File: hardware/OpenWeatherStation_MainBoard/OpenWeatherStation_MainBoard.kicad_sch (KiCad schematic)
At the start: 0 parts

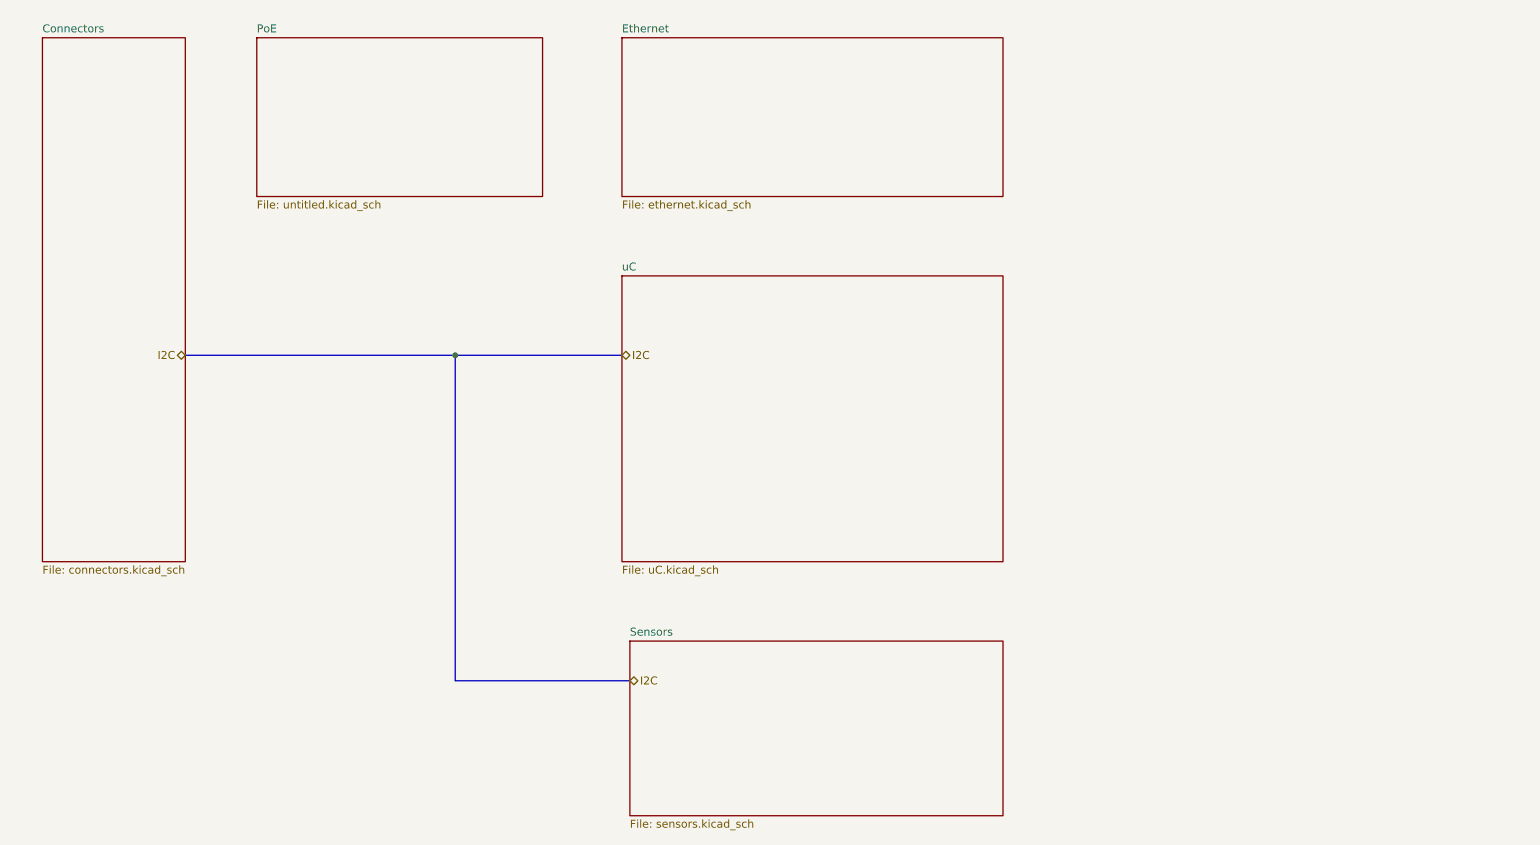
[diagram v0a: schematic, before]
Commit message: fix hierarchical bus
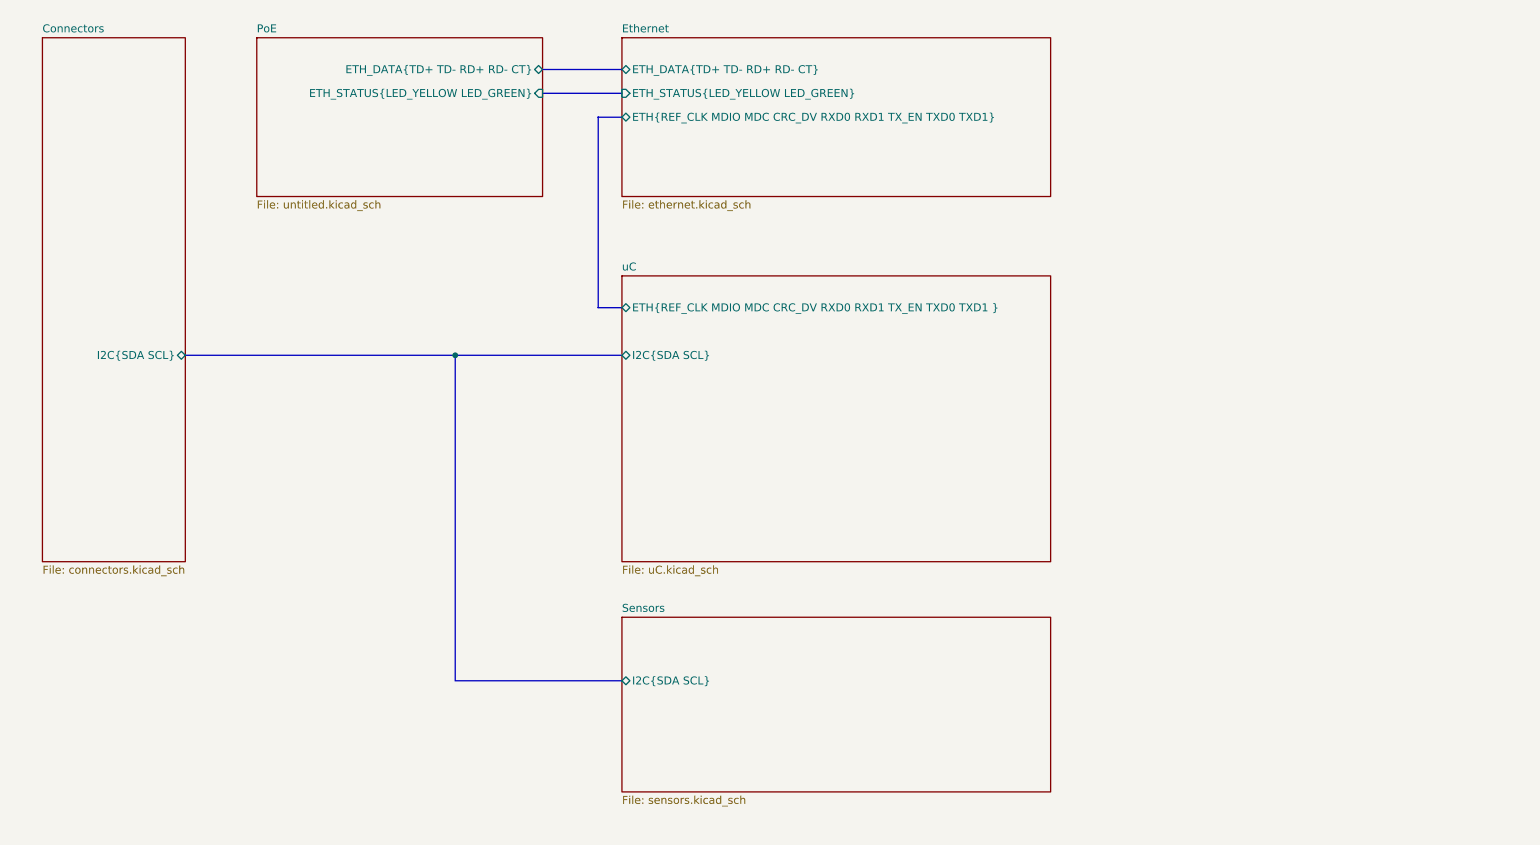
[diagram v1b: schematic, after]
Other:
- sheet Connectors ports: added I2C{SDA SCL}; removed none
- sheet Ethernet ports: added ETH_DATA{TD+ TD- RD+ RD- CT}, ETH_STATUS{LED_YELLOW LED_GREEN}, ETH{REF_CLK MDIO MDC CRC_DV RXD0 RXD1 TX_EN TXD0 TXD1}; removed none
- sheet PoE ports: added ETH_DATA{TD+ TD- RD+ RD- CT}, ETH_STATUS{LED_YELLOW LED_GREEN}; removed none
- sheet Sensors ports: added I2C{SDA SCL}; removed none
- sheet uC ports: added ETH{REF_CLK MDIO MDC CRC_DV RXD0 RXD1 TX_EN TXD0 TXD1 }, I2C{SDA SCL}; removed none
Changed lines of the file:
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@@
     (stroke (width 0) (type default))
   )
-  (bus (pts (xy 82.55 134.62) (xy 110.49 134.62))
+  (bus (pts (xy 105.41 44.45) (xy 105.41 74.93))
+    (stroke (width 0) (type default))
+  )
+  (bus (pts (xy 96.52 36.83) (xy 109.22 36.83))
+    (stroke (width 0) (type default))
+  )
+  (bus (pts (xy 109.22 44.45) (xy 105.41 44.45))
+    (stroke (width 0) (type default))
+  )
+  (bus (pts (xy 105.41 74.93) (xy 109.22 74.93))
+    (stroke (width 0) (type default))
+  )
+  (bus (pts (xy 82.55 134.62) (xy 109.22 134.62))
+    (stroke (width 0) (type default))
+  )
+  (bus (pts (xy 96.52 40.64) (xy 109.22 40.64))
     (stroke (width 0) (type default))
   )
@@
     (stroke (width 0) (type default))
   )
-  (hierarchical_label "I2C" (shape bidirectional) (at 109.22 82.55 0) (fields_autoplaced)
-    (effects (font (size 1.27 1.27)) (justify left))
-  )
-  (hierarchical_label "I2C" (shape bidirectional) (at 110.49 134.62 0) (fields_autoplaced)
-    (effects (font (size 1.27 1.27)) (justify left))
-  )
-  (hierarchical_label "I2C" (shape bidirectional) (at 39.37 82.55 180) (fields_autoplaced)
-    (effects (font (size 1.27 1.27)) (justify right))
-  )
-  (sheet (at 109.22 31.75) (size 60.96 25.4) (fields_autoplaced)
+  (sheet (at 109.22 31.75) (size 68.58 25.4) (fields_autoplaced)
     (stroke (width 0.1524) (type solid))
     (fill (color 0 0 0 0.0000))
@@
     (property "Sheetfile" "ethernet.kicad_sch" (at 109.22 57.7346 0)
       (effects (font (size 1.27 1.27)) (justify left top))
+    )
+    (pin "ETH_STATUS{LED_YELLOW LED_GREEN}" input (at 109.22 40.64 180)
+      (effects (font (size 1.27 1.27)) (justify left))
+    )
+    (pin "ETH_DATA{TD+ TD- RD+ RD- CT}" bidirectional (at 109.22 36.83 180)
+      (effects (font (size 1.27 1.27)) (justify left))
+    )
+    (pin "ETH{REF_CLK MDIO MDC CRC_DV RXD0 RXD1 TX_EN TXD0 TXD1}" bidirectional (at 109.22 44.45 180)
+      (effects (font (size 1.27 1.27)) (justify left))
     )
     (instances
@@
       (effects (font (size 1.27 1.27)) (justify left top))
     )
+    (pin "I2C{SDA SCL}" bidirectional (at 39.37 82.55 0)
+      (effects (font (size 1.27 1.27)) (justify right))
+    )
     (instances
       (project "OpenWeatherStation_MainBoard"
@@
       (effects (font (size 1.27 1.27)) (justify left top))
     )
+    (pin "ETH_STATUS{LED_YELLOW LED_GREEN}" input (at 96.52 40.64 0)
+      (effects (font (size 1.27 1.27)) (justify right))
+    )
+    (pin "ETH_DATA{TD+ TD- RD+ RD- CT}" bidirectional (at 96.52 36.83 0)
+      (effects (font (size 1.27 1.27)) (justify right))
+    )
     (instances
       (project "OpenWeatherStation_MainBoard"
@@
     )
   )
-  (sheet (at 110.49 128.27) (size 59.69 27.94) (fields_autoplaced)
+  (sheet (at 109.22 124.46) (size 68.58 27.94) (fields_autoplaced)
     (stroke (width 0.1524) (type solid))
     (fill (color 0 0 0 0.0000))
-    (property "Sheetname" "Sensors" (at 110.49 127.5584 0)
+    (property "Sheetname" "Sensors" (at 109.22 123.7484 0)
       (effects (font (size 1.27 1.27)) (justify left bottom))
     )
-    (property "Sheetfile" "sensors.kicad_sch" (at 110.49 156.7946 0)
+    (property "Sheetfile" "sensors.kicad_sch" (at 109.22 152.9846 0)
       (effects (font (size 1.27 1.27)) (justify left top))
+    )
+    (pin "I2C{SDA SCL}" bidirectional (at 109.22 134.62 180)
+      (effects (font (size 1.27 1.27)) (justify left))
     )
     (instances
@@
     )
   )
-  (sheet (at 109.22 69.85) (size 60.96 45.72) (fields_autoplaced)
+  (sheet (at 109.22 69.85) (size 68.58 45.72) (fields_autoplaced)
     (stroke (width 0.1524) (type solid))
     (fill (color 0 0 0 0.0000))
@@
       (effects (font (size 1.27 1.27)) (justify left top))
     )
+    (pin "I2C{SDA SCL}" bidirectional (at 109.22 82.55 180)
+      (effects (font (size 1.27 1.27)) (justify left))
+    )
+    (pin "ETH{REF_CLK MDIO MDC CRC_DV RXD0 RXD1 TX_EN TXD0 TXD1 }" bidirectional (at 109.22 74.93 180)
+      (effects (font (size 1.27 1.27)) (justify left))
+    )
     (instances

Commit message: move eth connector to dedicated sheet
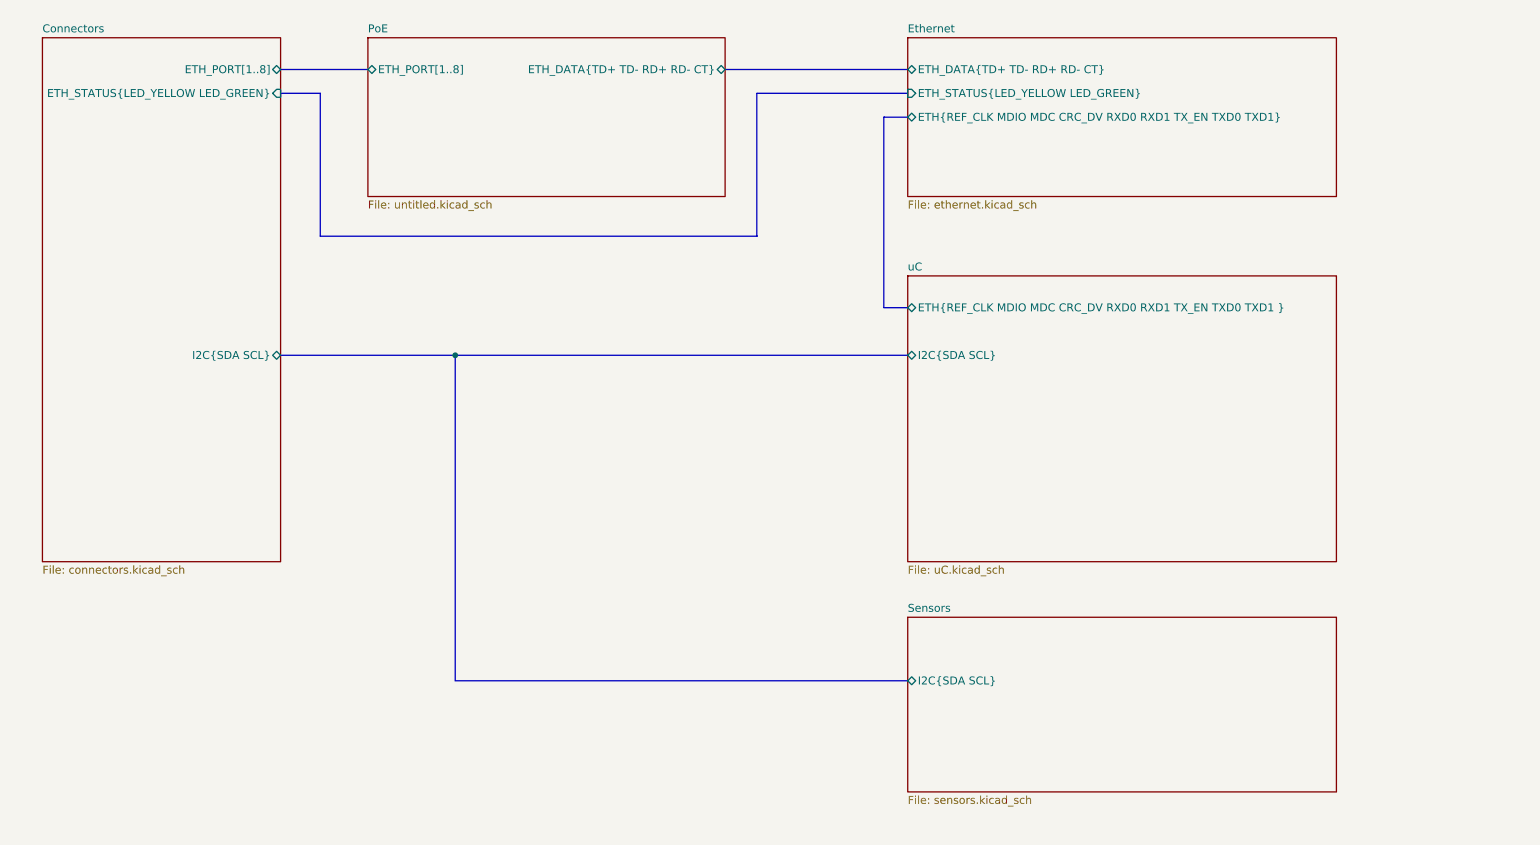
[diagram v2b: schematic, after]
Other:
- sheet Connectors ports: added ETH_PORT[1..8], ETH_STATUS{LED_YELLOW LED_GREEN}; removed none
- sheet PoE ports: added ETH_PORT[1..8]; removed ETH_STATUS{LED_YELLOW LED_GREEN}
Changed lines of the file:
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@@
     (stroke (width 0) (type default))
   )
-  (bus (pts (xy 39.37 82.55) (xy 82.55 82.55))
+  (bus (pts (xy 54.61 82.55) (xy 82.55 82.55))
     (stroke (width 0) (type default))
   )
-  (bus (pts (xy 105.41 44.45) (xy 105.41 74.93))
+  (bus (pts (xy 60.96 63.5) (xy 130.81 63.5))
     (stroke (width 0) (type default))
   )
-  (bus (pts (xy 96.52 36.83) (xy 109.22 36.83))
+  (bus (pts (xy 151.13 44.45) (xy 151.13 74.93))
     (stroke (width 0) (type default))
   )
-  (bus (pts (xy 109.22 44.45) (xy 105.41 44.45))
+  (bus (pts (xy 154.94 44.45) (xy 151.13 44.45))
     (stroke (width 0) (type default))
   )
-  (bus (pts (xy 105.41 74.93) (xy 109.22 74.93))
+  (bus (pts (xy 54.61 40.64) (xy 60.96 40.64))
     (stroke (width 0) (type default))
   )
-  (bus (pts (xy 82.55 134.62) (xy 109.22 134.62))
+  (bus (pts (xy 151.13 74.93) (xy 154.94 74.93))
     (stroke (width 0) (type default))
   )
-  (bus (pts (xy 96.52 40.64) (xy 109.22 40.64))
+  (bus (pts (xy 82.55 134.62) (xy 154.94 134.62))
     (stroke (width 0) (type default))
   )
-  (bus (pts (xy 109.22 82.55) (xy 82.55 82.55))
+  (bus (pts (xy 54.61 36.83) (xy 68.58 36.83))
     (stroke (width 0) (type default))
   )
-  (sheet (at 109.22 31.75) (size 68.58 25.4) (fields_autoplaced)
+  (bus (pts (xy 130.81 63.5) (xy 130.81 40.64))
+    (stroke (width 0) (type default))
+  )
+  (bus (pts (xy 130.81 40.64) (xy 154.94 40.64))
+    (stroke (width 0) (type default))
+  )
+  (bus (pts (xy 60.96 40.64) (xy 60.96 63.5))
+    (stroke (width 0) (type default))
+  )
+  (bus (pts (xy 154.94 82.55) (xy 82.55 82.55))
+    (stroke (width 0) (type default))
+  )
+  (bus (pts (xy 125.73 36.83) (xy 154.94 36.83))
+    (stroke (width 0) (type default))
+  )
+  (sheet (at 154.94 31.75) (size 68.58 25.4) (fields_autoplaced)
     (stroke (width 0.1524) (type solid))
     (fill (color 0 0 0 0.0000))
-    (property "Sheetname" "Ethernet" (at 109.22 31.0384 0)
+    (property "Sheetname" "Ethernet" (at 154.94 31.0384 0)
       (effects (font (size 1.27 1.27)) (justify left bottom))
     )
-    (property "Sheetfile" "ethernet.kicad_sch" (at 109.22 57.7346 0)
+    (property "Sheetfile" "ethernet.kicad_sch" (at 154.94 57.7346 0)
       (effects (font (size 1.27 1.27)) (justify left top))
     )
-    (pin "ETH_STATUS{LED_YELLOW LED_GREEN}" input (at 109.22 40.64 180)
+    (pin "ETH_STATUS{LED_YELLOW LED_GREEN}" input (at 154.94 40.64 180)
       (effects (font (size 1.27 1.27)) (justify left))
     )
-    (pin "ETH_DATA{TD+ TD- RD+ RD- CT}" bidirectional (at 109.22 36.83 180)
+    (pin "ETH_DATA{TD+ TD- RD+ RD- CT}" bidirectional (at 154.94 36.83 180)
       (effects (font (size 1.27 1.27)) (justify left))
     )
-    (pin "ETH{REF_CLK MDIO MDC CRC_DV RXD0 RXD1 TX_EN TXD0 TXD1}" bidirectional (at 109.22 44.45 180)
+    (pin "ETH{REF_CLK MDIO MDC CRC_DV RXD0 RXD1 TX_EN TXD0 TXD1}" bidirectional (at 154.94 44.45 180)
       (effects (font (size 1.27 1.27)) (justify left))
     )
@@
     )
   )
-  (sheet (at 16.51 31.75) (size 22.86 83.82) (fields_autoplaced)
+  (sheet (at 16.51 31.75) (size 38.1 83.82) (fields_autoplaced)
     (stroke (width 0.1524) (type solid))
     (fill (color 0 0 0 0.0000))
@@
       (effects (font (size 1.27 1.27)) (justify left top))
     )
-    (pin "I2C{SDA SCL}" bidirectional (at 39.37 82.55 0)
+    (pin "I2C{SDA SCL}" bidirectional (at 54.61 82.55 0)
+      (effects (font (size 1.27 1.27)) (justify right))
+    )
+    (pin "ETH_PORT[1..8]" bidirectional (at 54.61 36.83 0)
+      (effects (font (size 1.27 1.27)) (justify right))
+    )
+    (pin "ETH_STATUS{LED_YELLOW LED_GREEN}" input (at 54.61 40.64 0)
       (effects (font (size 1.27 1.27)) (justify right))
     )
@@
     )
   )
-  (sheet (at 50.8 31.75) (size 45.72 25.4) (fields_autoplaced)
+  (sheet (at 68.58 31.75) (size 57.15 25.4) (fields_autoplaced)
     (stroke (width 0.1524) (type solid))
     (fill (color 0 0 0 0.0000))
-    (property "Sheetname" "PoE" (at 50.8 31.0384 0)
+    (property "Sheetname" "PoE" (at 68.58 31.0384 0)
       (effects (font (size 1.27 1.27)) (justify left bottom))
     )
-    (property "Sheetfile" "untitled.kicad_sch" (at 50.8 57.7346 0)
+    (property "Sheetfile" "untitled.kicad_sch" (at 68.58 57.7346 0)
       (effects (font (size 1.27 1.27)) (justify left top))
     )
-    (pin "ETH_STATUS{LED_YELLOW LED_GREEN}" input (at 96.52 40.64 0)
-      (effects (font (size 1.27 1.27)) (justify right))
+    (pin "ETH_PORT[1..8]" bidirectional (at 68.58 36.83 180)
+      (effects (font (size 1.27 1.27)) (justify left))
     )
-    (pin "ETH_DATA{TD+ TD- RD+ RD- CT}" bidirectional (at 96.52 36.83 0)
+    (pin "ETH_DATA{TD+ TD- RD+ RD- CT}" bidirectional (at 125.73 36.83 0)
       (effects (font (size 1.27 1.27)) (justify right))
     )
@@
     )
   )
-  (sheet (at 109.22 124.46) (size 68.58 27.94) (fields_autoplaced)
+  (sheet (at 154.94 124.46) (size 68.58 27.94) (fields_autoplaced)
     (stroke (width 0.1524) (type solid))
     (fill (color 0 0 0 0.0000))
-    (property "Sheetname" "Sensors" (at 109.22 123.7484 0)
+    (property "Sheetname" "Sensors" (at 154.94 123.7484 0)
       (effects (font (size 1.27 1.27)) (justify left bottom))
     )
-    (property "Sheetfile" "sensors.kicad_sch" (at 109.22 152.9846 0)
+    (property "Sheetfile" "sensors.kicad_sch" (at 154.94 152.9846 0)
       (effects (font (size 1.27 1.27)) (justify left top))
     )
-    (pin "I2C{SDA SCL}" bidirectional (at 109.22 134.62 180)
+    (pin "I2C{SDA SCL}" bidirectional (at 154.94 134.62 180)
       (effects (font (size 1.27 1.27)) (justify left))
     )
@@
     )
   )
-  (sheet (at 109.22 69.85) (size 68.58 45.72) (fields_autoplaced)
+  (sheet (at 154.94 69.85) (size 68.58 45.72) (fields_autoplaced)
     (stroke (width 0.1524) (type solid))
     (fill (color 0 0 0 0.0000))
-    (property "Sheetname" "uC" (at 109.22 69.1384 0)
+    (property "Sheetname" "uC" (at 154.94 69.1384 0)
       (effects (font (size 1.27 1.27)) (justify left bottom))
     )
-    (property "Sheetfile" "uC.kicad_sch" (at 109.22 116.1546 0)
+    (property "Sheetfile" "uC.kicad_sch" (at 154.94 116.1546 0)
       (effects (font (size 1.27 1.27)) (justify left top))
     )
-    (pin "I2C{SDA SCL}" bidirectional (at 109.22 82.55 180)
+    (pin "I2C{SDA SCL}" bidirectional (at 154.94 82.55 180)
       (effects (font (size 1.27 1.27)) (justify left))
     )
-    (pin "ETH{REF_CLK MDIO MDC CRC_DV RXD0 RXD1 TX_EN TXD0 TXD1 }" bidirectional (at 109.22 74.93 180)
+    (pin "ETH{REF_CLK MDIO MDC CRC_DV RXD0 RXD1 TX_EN TXD0 TXD1 }" bidirectional (at 154.94 74.93 180)
       (effects (font (size 1.27 1.27)) (justify left))
     )
